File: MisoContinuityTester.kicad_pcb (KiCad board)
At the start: 2 copper layers, 130.5 x 66 mm, 15 parts, among them J10 OUTPUT, J11 OUTPUT, J12 TYPE1, J13 TYPE2, J3 POWER SWITCH, J4 INPUT, J5 INPUT, J6 FAIL, J7 PASS, J8 POWER 5V-12V, J9 START

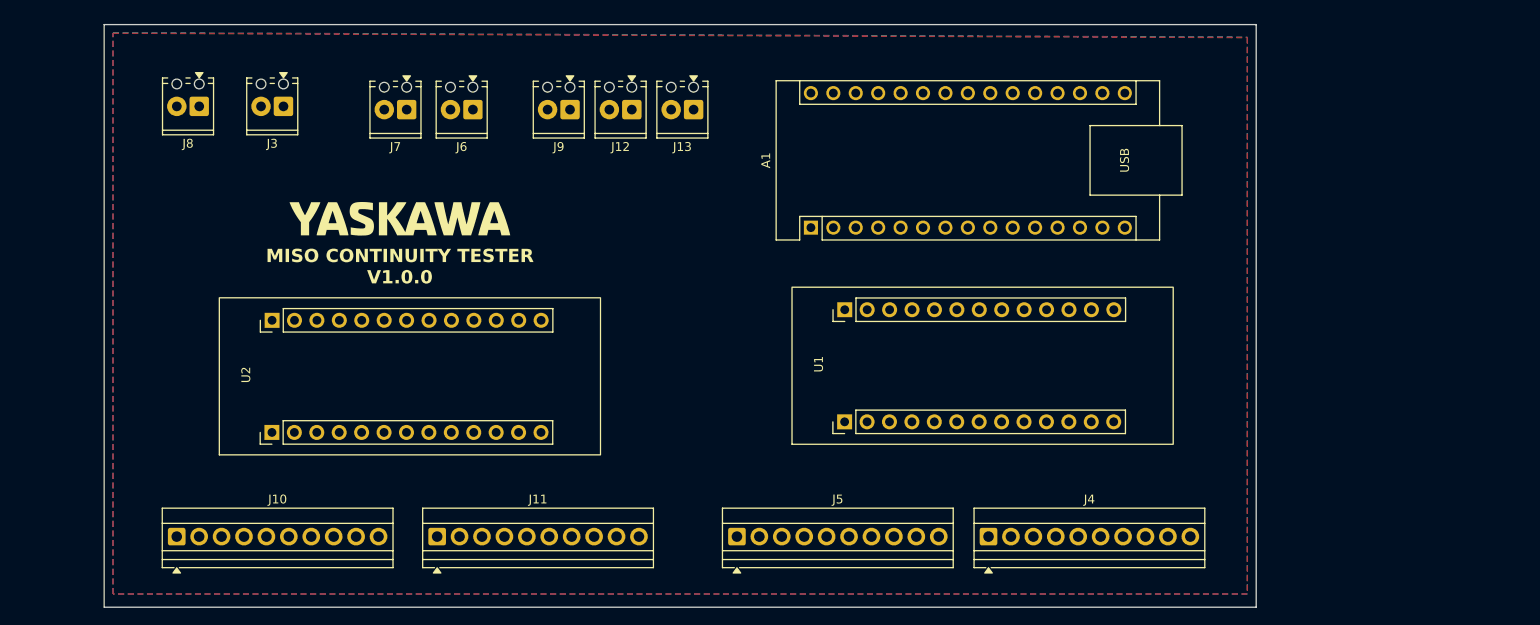
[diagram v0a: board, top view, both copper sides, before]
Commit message: added mounting holes
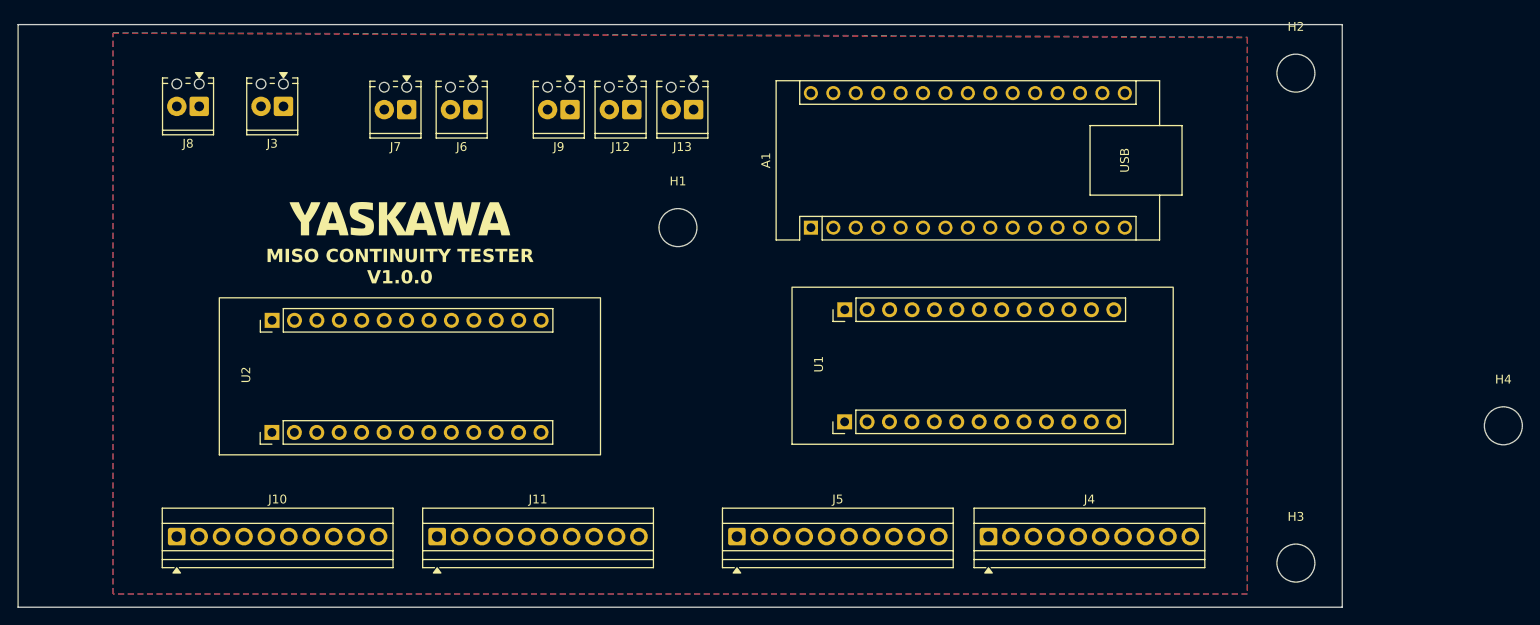
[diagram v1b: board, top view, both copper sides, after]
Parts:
- added H1: MountingHole, MountingHole:MountingHole_4.3mm_M4, F.Cu at (124.5, 82.0)
- added H2: MountingHole, MountingHole:MountingHole_4.3mm_M4, F.Cu at (194.5, 64.5)
- added H3: MountingHole, MountingHole:MountingHole_4.3mm_M4, F.Cu at (194.5, 120.0)
- added H4: MountingHole, MountingHole:MountingHole_4.3mm_M4, F.Cu at (218.0, 104.5)
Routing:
- added copper zone on F.Cu, net +5V
- removed copper zone on F.Cu, net VCC
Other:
- board size 130.5 x 66 mm -> 150 x 66 mm

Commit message: wired everything up and added resistors for pass and fail
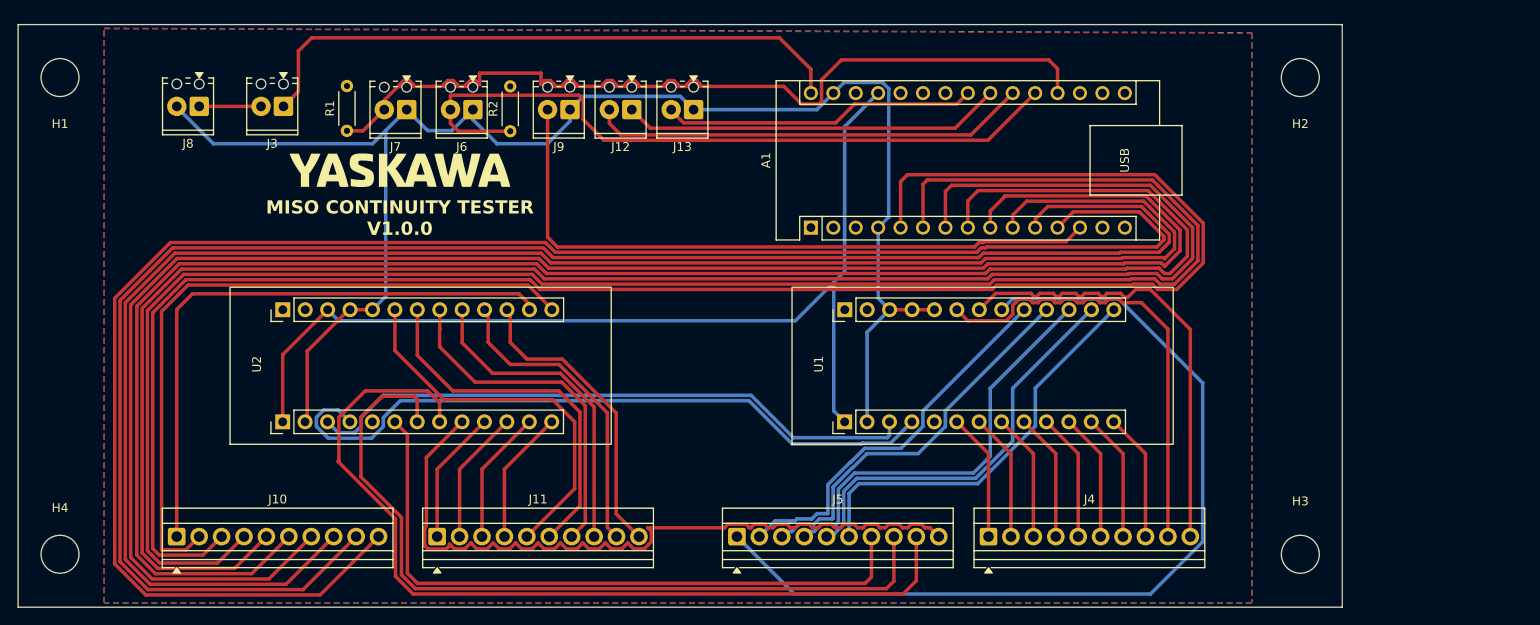
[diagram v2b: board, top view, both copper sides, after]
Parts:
- added R1: R_US, Resistor_THT:R_Axial_DIN0204_L3.6mm_D1.6mm_P5.08mm_Horizontal, F.Cu at (87.0, 71.0)
- added R2: R_US, Resistor_THT:R_Axial_DIN0204_L3.6mm_D1.6mm_P5.08mm_Horizontal, F.Cu at (105.5, 71.1)
- moved H4 164.1 mm to (54.5, 119.0)
- moved H1 72.0 mm to (54.5, 65.0), turned to 180 degrees
- moved G*** 5.50 mm to (93.0, 75.5)
- moved U2 1.71 mm to (79.7, 104.0)
- moved H3 1.12 mm to (195.0, 119.0)
- moved H2 0.71 mm to (195.0, 65.0), turned to 180 degrees
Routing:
- net /B13: track 0.00 -> 205.6 mm
- net /B14: track 0.00 -> 205.1 mm
- net /B15: track 0.00 -> 204.6 mm
- net /B16: track 0.00 -> 204.0 mm
- net /B17: track 0.00 -> 202.8 mm
- net /B18: track 0.00 -> 202.2 mm
- net /B19: track 0.00 -> 201.6 mm
- net /B20: track 0.00 -> 201.0 mm
- net GND: track 0.00 -> 178.1 mm
- net +5V: track 0.00 -> 114.3 mm
- net /A11: track 0.00 -> 103.1 mm
- net /A19: track 0.00 -> 101.6 mm
- net /PASS: track 0.00 -> 100.6 mm
- net /A18: track 0.00 -> 91.6 mm
- net /A20: track 0.00 -> 85.2 mm
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
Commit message: added lables
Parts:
- J3: value POWER SWITCH -> PW SWITCH
- J8: value POWER 5V-12V -> PW 5V-12V
- moved J3 0.23 mm to (79.8, 68.5)
- moved J8 0.23 mm to (70.3, 68.5)
- renumbered H4 to H3, H3 to H4
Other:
- board text added: "A1"
- board text added: "A10"
- board text added: "A11"
- board text added: "A12"
- board text added: "A13"
- board text added: "A14"
- board text added: "A15"
- board text added: "A16"
- board text added: "A17"
- board text added: "A18"
- board text added: "A19"
- board text added: "A2"
- board text added: "A20"
- board text added: "A3"
- board text added: "A4"
- board text added: "A5"
- board text added: "A6"
- board text added: "A7"
- board text added: "A8"
- board text added: "A9"
- board text added: "B1"
- board text added: "B10"
- board text added: "B11"
- board text added: "B12"
- board text added: "B13"
- board text added: "B14"
- board text added: "B15"
- board text added: "B16"
- board text added: "B17"
- board text added: "B18"
- board text added: "B19"
- board text added: "B2"
- board text added: "B20"
- board text added: "B3"
- board text added: "B4"
- board text added: "B5"
- board text added: "B6"
- board text added: "B7"
- board text added: "B8"
- board text added: "B9"
- board text added: "Expander 1"
- board text added: "Expander 2"
- board text added: "GND"
